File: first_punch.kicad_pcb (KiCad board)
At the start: 2 copper layers, 162.6 x 99.1 mm, 67 parts, among them J1 AudioJack3, J2 Barrel_Jack_Switch, Q1 2N3904, SW1 SMTS-102, SW2 SMTS-102, SW3 SMTS-102, U1 40106, U3 LM358

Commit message: Finish circuit and pcb
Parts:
- removed J1: AudioJack3, Import:PJ302M
- added D9: LED, LED_THT:LED_D5.0mm, F.Cu at (157.5, 73.7)
- added J3: ~, Import:PJ302M, F.Cu at (152.4, 41.5)
- added R27: 10k, Resistor_THT:R_Axial_DIN0207_L6.3mm_D2.5mm_P10.16mm_Horizontal, F.Cu at (158.8, 68.6)
- added REF**: Polarity_Center_Positive_6mm_SilkScreen, Symbol:Polarity_Center_Positive_6mm_SilkScreen, F.Cu at (167.6, 71.1)
- SW1, SW2, SW3: footprint V:SIP3 -> Import:SMTS-102
- moved D7 47.1 mm to (133.3, 108.0)
- moved R25 46.5 mm to (128.3, 107.9), turned to 90 degrees
- moved C14 35.8 mm to (146.1, 62.2)
- moved R24 33.6 mm to (45.7, 69.8)
- moved D6 32.6 mm to (40.6, 62.2), turned to 180 degrees
- moved RV12 17.0 mm to (99.1, 43.5)
- moved R19 16.5 mm to (132.1, 76.4)
- moved RV11 16.1 mm to (115.6, 43.5)
- moved C2 5.24 mm to (153.7, 78.7)
- moved SW2 3.81 mm to (39.4, 49.5), turned to 90 degrees
- moved R20 3.50 mm to (132.1, 60.5)
- moved D4 2.84 mm to (151.1, 76.2)
- moved SW3 2.84 mm to (39.4, 96.5), turned to 90 degrees
- moved D8 2.54 mm to (66.0, 94.0), turned to 180 degrees
- moved R23 2.54 mm to (147.3, 76.2)
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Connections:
- RV1 pad 1: Net-(R1-Pad2) -> Net-(D6-A)
- RV1 pad 3: Net-(D6-A) -> Net-(R1-Pad2)
- RV2 pad 1: Net-(R8-Pad2) -> Net-(R13-Pad1)
- RV2 pad 3: Net-(R13-Pad1) -> Net-(R8-Pad2)
- RV3 pad 1: Net-(R3-Pad2) -> Net-(D8-A)
- RV3 pad 3: Net-(D8-A) -> Net-(R3-Pad2)
- RV4 pad 1: Net-(SW1-C) -> GND
- RV4 pad 3: GND -> Net-(SW1-C)
- RV5 pad 1: Net-(R7-Pad2) -> Net-(Q1-C)
- RV5 pad 3: Net-(Q1-C) -> Net-(R7-Pad2)
- RV6 pad 1: Net-(R2-Pad2) -> Net-(D7-A)
- RV6 pad 3: Net-(D7-A) -> Net-(R2-Pad2)
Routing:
- net GND: track 22.5 -> 363.5 mm, vias 0 -> 1
- net +12V: track 0.00 -> 195.7 mm, vias 0 -> 1
- net Net-(D7-A): track 0.00 -> 124.3 mm
- net Net-(R10-Pad1): track 0.00 -> 122.9 mm
- net Net-(D1-K): track 0.00 -> 100.3 mm
- net Net-(C4-Pad1): track 0.00 -> 98.8 mm
- net Net-(R14-Pad1): track 0.00 -> 89.9 mm
- net Vref: track 0.00 -> 76.3 mm
- net Net-(R13-Pad1): track 0.00 -> 71.0 mm
- net Net-(SW1-C): track 0.00 -> 70.6 mm
- net Net-(R11-Pad1): track 11.2 -> 80.1 mm
- net Net-(D6-A): track 0.00 -> 61.8 mm
- net Net-(C12-Pad1): track 0.00 -> 57.6 mm
- net Net-(R19-Pad1): track 0.00 -> 56.2 mm
- net Net-(C12-Pad2): track 0.00 -> 56.0 mm
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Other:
- board size 162.6 x 99.1 mm -> 141 x 99.1 mm
- board text added: "Amount"
- board text added: "Cutoff Filter"
- board text added: "Freq"
- board text added: "LFO"
- board text added: "OSC1"
- board text added: "OSC2"
- board text added: "OSC3"
- board text added: "Res"

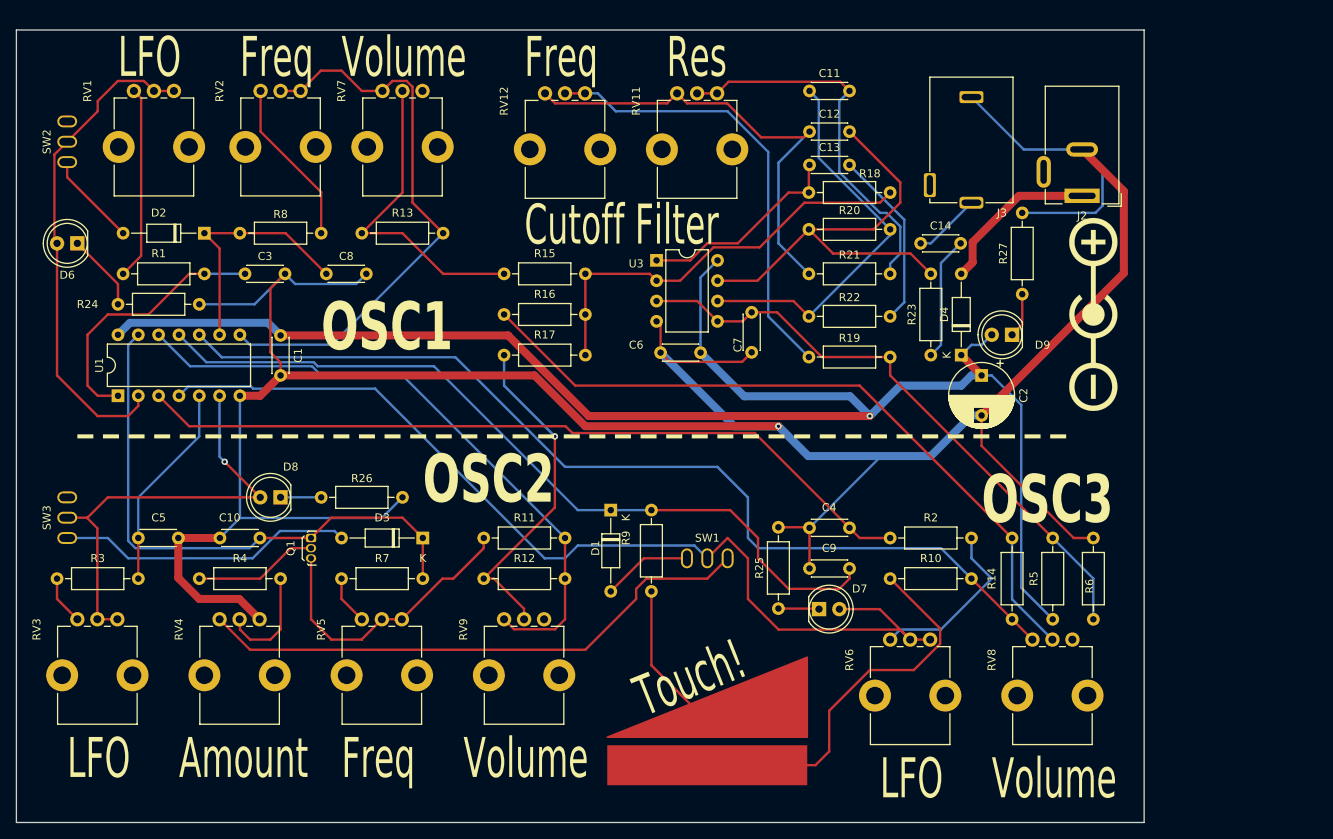
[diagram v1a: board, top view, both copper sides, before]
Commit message: add paints move ref resistors
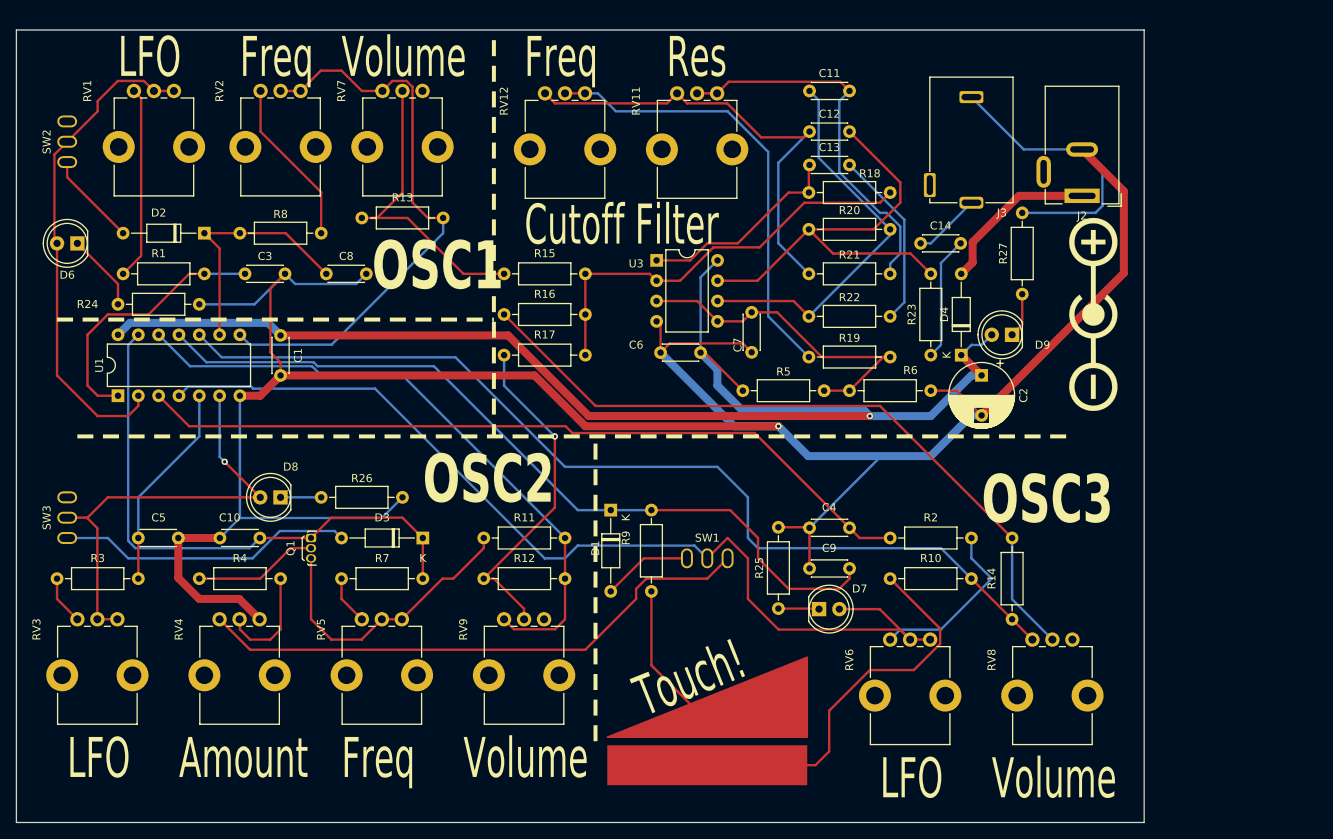
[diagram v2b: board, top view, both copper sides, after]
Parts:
- moved R5 48.1 mm to (123.8, 80.6), turned to 0 degrees
- moved R6 41.8 mm to (137.2, 80.6), turned to 0 degrees
- moved R13 1.91 mm to (86.4, 59.1)
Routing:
- net Vref: track 76.3 -> 43.0 mm
- net +12V: track 195.7 -> 169.3 mm
- net GND: track 363.5 -> 348.5 mm
- net Net-(R13-Pad2): track 39.8 -> 38.5 mm
- net Net-(R13-Pad1): track 71.0 -> 72.1 mm

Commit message: add mounting holes for M3 screws
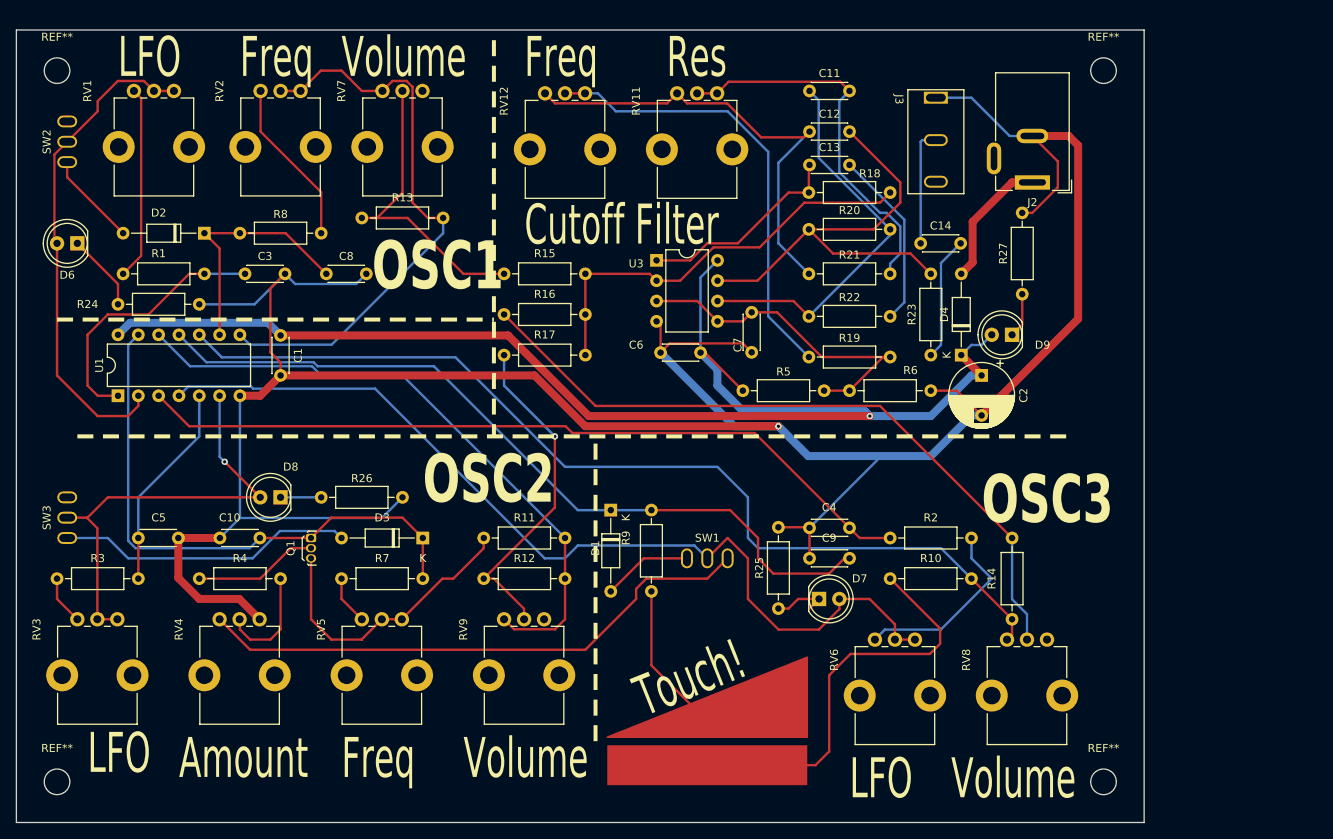
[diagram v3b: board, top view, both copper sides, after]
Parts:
- removed the REF** at (167.6, 71.1)
- added REF**: MountingHole_3.2mm_M3, MountingHole:MountingHole_3.2mm_M3, F.Cu at (38.1, 40.6)
- added REF**: MountingHole_3.2mm_M3, MountingHole:MountingHole_3.2mm_M3, F.Cu at (38.1, 129.5)
- added REF**: MountingHole_3.2mm_M3, MountingHole:MountingHole_3.2mm_M3, F.Cu at (168.9, 129.5)
- added REF**: MountingHole_3.2mm_M3, MountingHole:MountingHole_3.2mm_M3, F.Cu at (168.9, 40.6)
- D6, D7, D8: value LED -> LED green
- D9: value LED -> LED red
- J3: footprint Import:PJ302M -> Import:PJ-316
- moved J2 6.43 mm to (160.0, 54.6)
- moved J3 5.14 mm to (148.0, 44.0)
- moved RV8 3.18 mm to (156.8, 111.8)
- moved RV6 1.91 mm to (140.3, 111.8)
- moved C9 1.27 mm to (137.2, 101.6)
- moved D7 1.27 mm to (133.3, 106.7)
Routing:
- net Net-(D7-A): track 124.3 -> 117.6 mm
- net GND: track 348.5 -> 342.0 mm
- net Net-(C14-Pad1): track 8.45 -> 14.7 mm
- net Net-(D4-A): track 20.6 -> 16.6 mm
- net Net-(D5-Pad2): track 49.1 -> 51.7 mm
- net Net-(D7-K): track 5.11 -> 7.27 mm
- net Net-(R2-Pad2): track 22.0 -> 23.9 mm
- net Net-(D1-K): track 100.3 -> 98.5 mm
- net Net-(R14-Pad1): track 89.9 -> 88.5 mm
- net Net-(R10-Pad1): track 122.9 -> 122.1 mm

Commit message: add text - Ver1 - symbol for power supply - title - text on rear
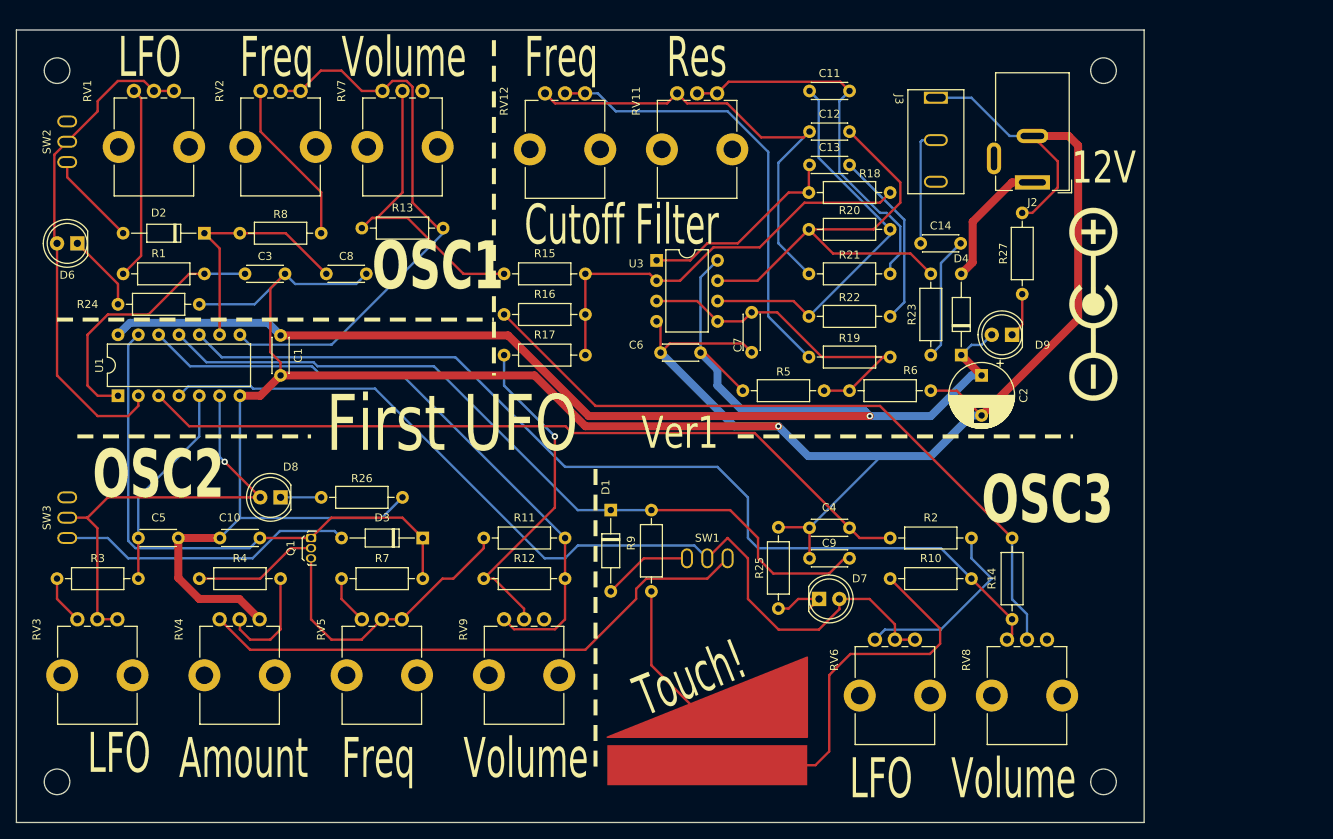
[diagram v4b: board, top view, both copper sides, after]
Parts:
- added REF**: Polarity_Center_Positive_6mm_SilkScreen, Symbol:Polarity_Center_Positive_6mm_SilkScreen, F.Cu at (167.6, 69.8)
- moved R13 1.27 mm to (86.4, 60.3)
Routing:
- net Net-(R13-Pad1): track 72.1 -> 71.4 mm
- net Net-(R13-Pad2): track 38.5 -> 39.0 mm
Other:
- board text added: "12V"
- board text added: "First UFO"
- board text added: "Thanks to Ray Wilson and his website musicfromouterspace.com. I took most of the ideas from his Weird Sound Generator, but added a few from other places."
- board text added: "Ver1"
- board text added: "original circuit on github.com/paltus23/first_punch"
